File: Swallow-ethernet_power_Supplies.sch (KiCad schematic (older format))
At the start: 29 parts, among them P7 +5V_In, P8 V_In, U12 NCP1529, U13 NCP1529, U14 NCP303LSN09T1G

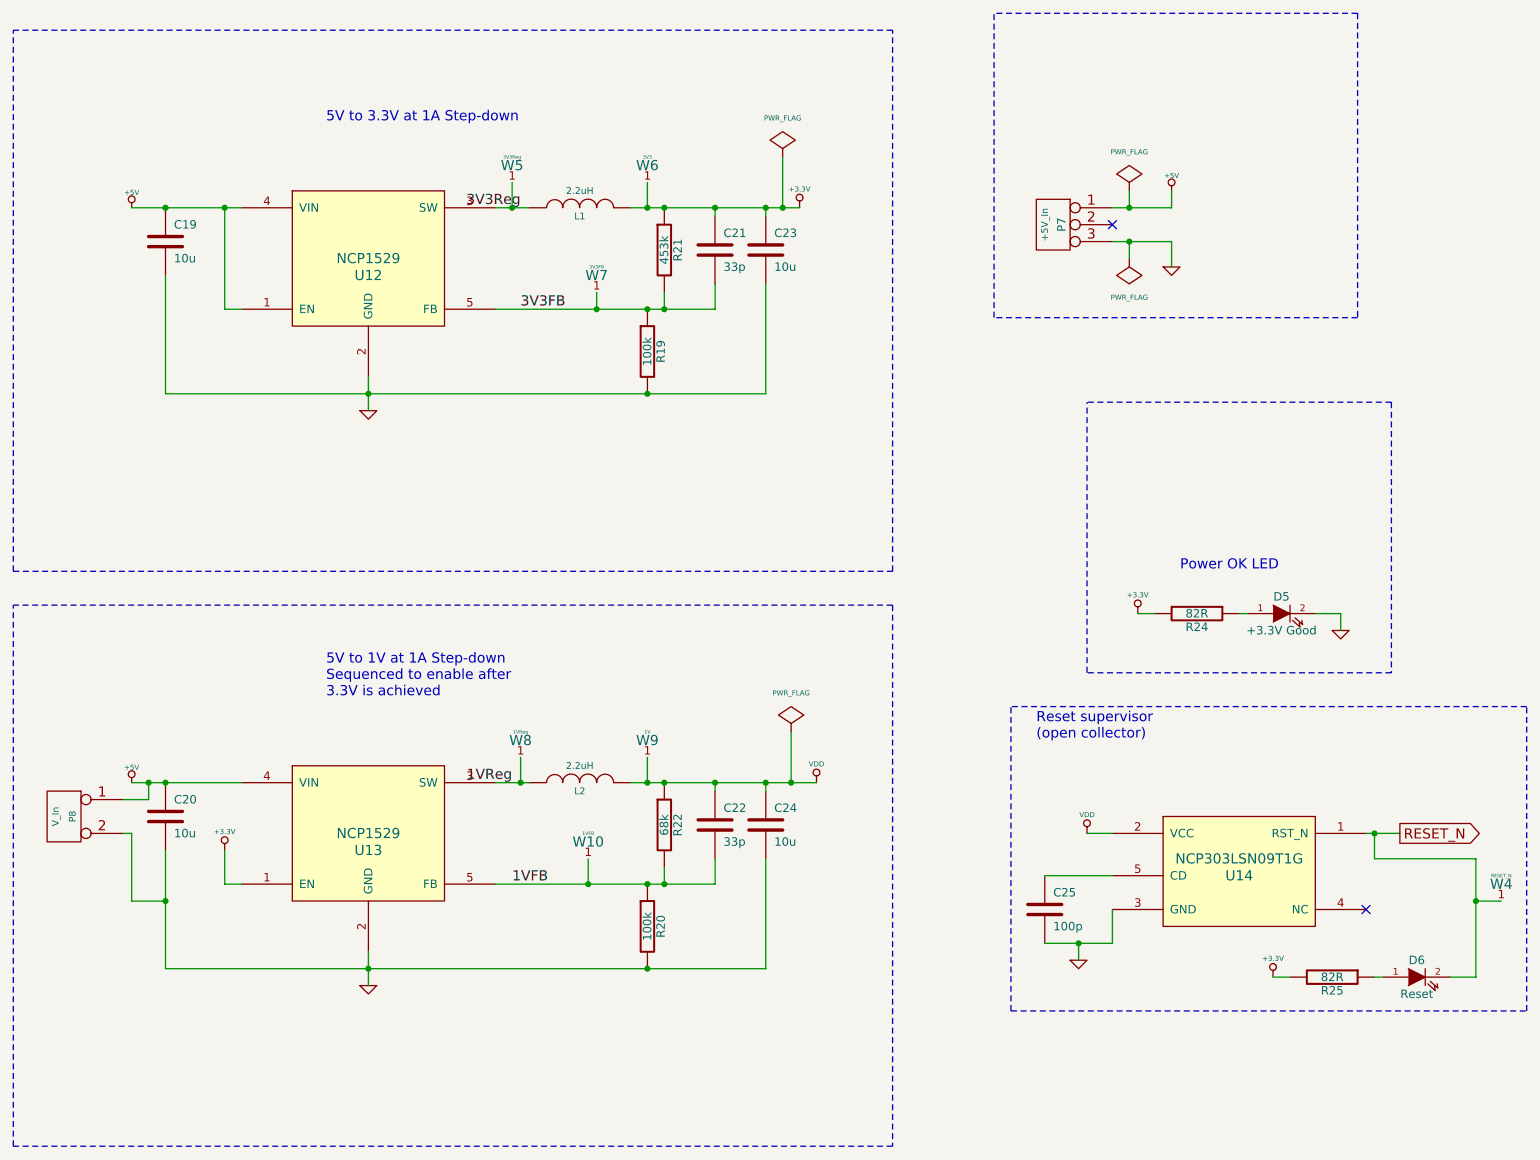
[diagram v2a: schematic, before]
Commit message: Re-annotated schematic and deleted redundant components from PCB design.
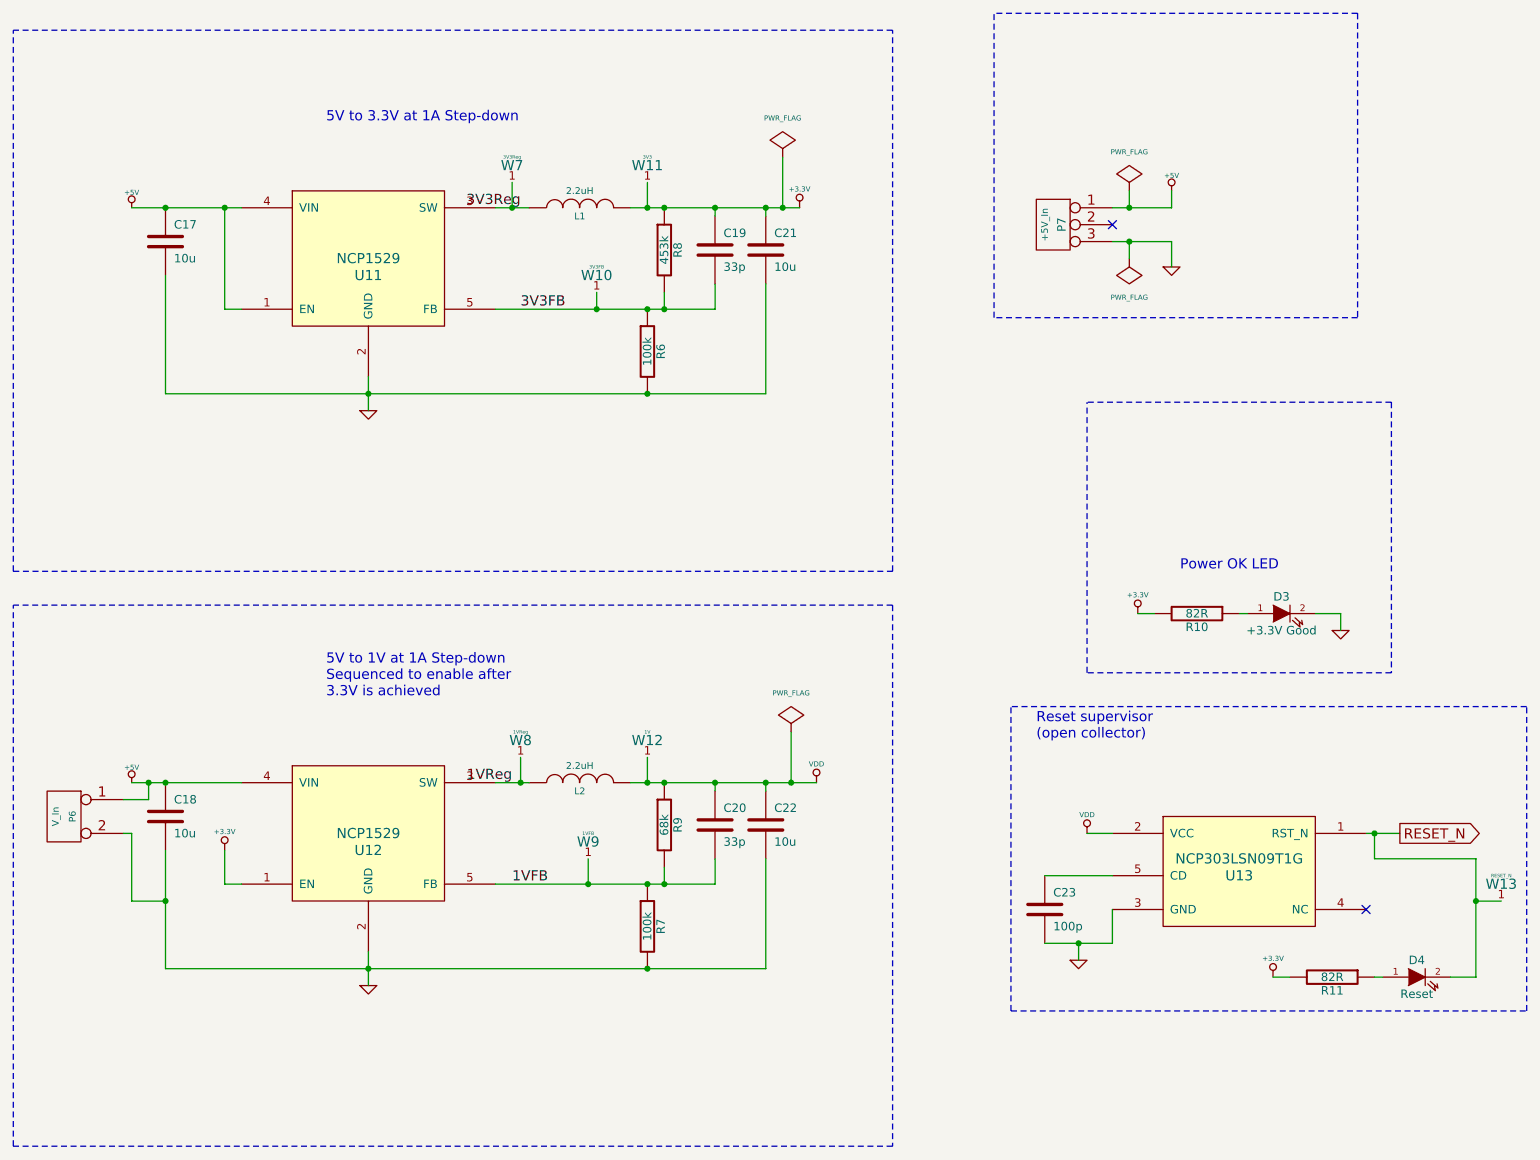
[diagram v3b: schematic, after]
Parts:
- renumbered C19 to C17, C20 to C18, C21 to C19, C22 to C20, C23 to C21, C24 to C22, C25 to C23, D5 to D3, D6 to D4, P8 to P6, R24 to R10, R25 to R11, R19 to R6, R20 to R7, R21 to R8, R22 to R9, U12 to U11, U13 to U12, U14 to U13, W7 to W10, W6 to W11, W9 to W12, W4 to W13, W5 to W7, W10 to W9
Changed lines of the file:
@@
-EESchema Schematic File Version 2  date 30/09/2012 22:11:50
+EESchema Schematic File Version 2  date 30/09/2012 22:23:08
 LIBS:power
 LIBS:device
@@
 NoConn ~ 7550 2100
 $Comp
-L CONN_2 P8
+L CONN_2 P6
 U 1 1 4F69BE5A
 P 1350 5600
-F 0 "P8" V 1300 5600 40  0000 C CNN
+F 0 "P6" V 1300 5600 40  0000 C CNN
 F 1 "V_In" V 1400 5600 40  0000 C CNN
 	1    1350 5600
@@
 $EndComp
 $Comp
-L TESTPOINT W10
+L TESTPOINT W9
 U 1 1 4F5FB79A
 P 4450 5700
-F 0 "W10" H 4450 5650 60  0000 C CNN
+F 0 "W9" H 4450 5650 60  0000 C CNN
 F 1 "1VFB" H 4450 5700 20  0000 C CNN
 F 2 "TestPad-1mm" H 4450 5800 20  0001 C CNN
@@
 $EndComp
 $Comp
-L TESTPOINT W9
+L TESTPOINT W12
 U 1 1 4F5FB796
 P 4800 5100
-F 0 "W9" H 4800 5050 60  0000 C CNN
+F 0 "W12" H 4800 5050 60  0000 C CNN
 F 1 "1V" H 4800 5100 20  0000 C CNN
 F 2 "TestPad-1mm" H 4800 5200 20  0001 C CNN
@@
 $EndComp
 $Comp
-L TESTPOINT W7
+L TESTPOINT W10
 U 1 1 4F5FB764
 P 4500 2350
-F 0 "W7" H 4500 2300 60  0000 C CNN
+F 0 "W10" H 4500 2300 60  0000 C CNN
 F 1 "3V3FB" H 4500 2350 20  0000 C CNN
 F 2 "TestPad-1mm" H 4500 2450 20  0001 C CNN
@@
 $EndComp
 $Comp
-L TESTPOINT W6
+L TESTPOINT W11
 U 1 1 4F5FB75E
 P 4800 1700
-F 0 "W6" H 4800 1650 60  0000 C CNN
+F 0 "W11" H 4800 1650 60  0000 C CNN
 F 1 "3V3" H 4800 1700 20  0000 C CNN
 F 2 "TestPad-1mm" H 4800 1800 20  0001 C CNN
@@
 $EndComp
 $Comp
-L TESTPOINT W5
+L TESTPOINT W7
 U 1 1 4F5FB74C
 P 4000 1700
-F 0 "W5" H 4000 1650 60  0000 C CNN
+F 0 "W7" H 4000 1650 60  0000 C CNN
 F 1 "3V3Reg" H 4000 1700 20  0000 C CNN
 F 2 "TestPad-1mm" H 4000 1800 20  0001 C CNN
@@
 $EndComp
 $Comp
-L +3.3V #PWR085
+L +3.3V #PWR061
 U 1 1 4F5FB6A5
 P 2300 5800
-F 0 "#PWR085" H 2300 5760 30  0001 C CNN
+F 0 "#PWR061" H 2300 5760 30  0001 C CNN
 F 1 "+3.3V" H 2300 5910 30  0000 C CNN
 	1    2300 5800
@@
 1VReg
 $Comp
-L TESTPOINT W4
+L TESTPOINT W13
 U 1 1 4F5B5145
 P 9850 5950
-F 0 "W4" H 9850 5900 60  0000 C CNN
+F 0 "W13" H 9850 5900 60  0000 C CNN
 F 1 "RESET_N" H 9850 5950 20  0000 C CNN
 F 2 "TestPad-1mm" H 9850 6050 20  0001 C CNN
@@
 $EndComp
 $Comp
-L R R25
+L R R11
 U 1 1 4F5B50F0
 P 8850 6550
-F 0 "R25" V 8930 6550 50  0000 C CNN
+F 0 "R11" V 8930 6550 50  0000 C CNN
 F 1 "82R" V 8850 6550 50  0000 C CNN
 F 2 "SM0402" H 8850 6550 60  0001 C CNN
@@
 $EndComp
 $Comp
-L LED D6
+L LED D4
 U 1 1 4F5B50EF
 P 9350 6550
-F 0 "D6" H 9350 6650 50  0000 C CNN
+F 0 "D4" H 9350 6650 50  0000 C CNN
 F 1 "Reset" H 9350 6450 50  0000 C CNN
 F 2 "X_LED-0603" H 9350 6550 60  0001 C CNN
@@
 $EndComp
 $Comp
-L +3.3V #PWR086
+L +3.3V #PWR062
 U 1 1 4F5B50EE
 P 8500 6550
-F 0 "#PWR086" H 8500 6510 30  0001 C CNN
+F 0 "#PWR062" H 8500 6510 30  0001 C CNN
 F 1 "+3.3V" H 8500 6660 30  0000 C CNN
 	1    8500 6550
@@
 $EndComp
 $Comp
-L VDD #PWR087
+L VDD #PWR063
 U 1 1 4ED160AA
 P 5800 5400
-F 0 "#PWR087" H 5800 5500 30  0001 C CNN
+F 0 "#PWR063" H 5800 5500 30  0001 C CNN
 F 1 "VDD" H 5800 5510 30  0000 C CNN
 	1    5800 5400
@@
 NoConn ~ 9050 6150
 $Comp
-L GND #PWR088
+L GND #PWR064
 U 1 1 4EDA727F
 P 7350 6450
-F 0 "#PWR088" H 7350 6450 30  0001 C CNN
+F 0 "#PWR064" H 7350 6450 30  0001 C CNN
 F 1 "GND" H 7350 6380 30  0001 C CNN
 	1    7350 6450
@@
 $EndComp
 $Comp
-L VDD #PWR089
+L VDD #PWR065
 U 1 1 4EDA7272
 P 7400 5700
-F 0 "#PWR089" H 7400 5800 30  0001 C CNN
+F 0 "#PWR065" H 7400 5800 30  0001 C CNN
 F 1 "VDD" H 7400 5810 30  0000 C CNN
 	1    7400 5700
@@
 $EndComp
 $Comp
-L C C25
+L C C23
 U 1 1 4EDA724A
 P 7150 6150
-F 0 "C25" H 7200 6250 50  0000 L CNN
+F 0 "C23" H 7200 6250 50  0000 L CNN
 F 1 "100p" H 7200 6050 50  0000 L CNN
 F 2 "SM0402" H 7150 6150 60  0001 C CNN
@@
 $EndComp
 $Comp
-L NCP303 U14
+L NCP303 U13
 U 1 1 4EDA70F3
 P 8300 5950
-F 0 "U14" H 8300 5950 60  0000 C CNN
+F 0 "U13" H 8300 5950 60  0000 C CNN
 F 1 "NCP303LSN09T1G" H 8300 6050 60  0000 C CNN
 F 2 "TSOP-5" H 8300 5950 60  0001 C CNN
@@
 $EndComp
 $Comp
-L NCP1529 U13
+L NCP1529 U12
 U 1 1 4ED16424
 P 3150 5750
-F 0 "U13" H 3150 5700 60  0000 C CNN
+F 0 "U12" H 3150 5700 60  0000 C CNN
 F 1 "NCP1529" H 3150 5800 60  0000 C CNN
 F 2 "TSOP-5" H 3150 5750 60  0001 C CNN
@@
 $EndComp
 $Comp
-L GND #PWR090
+L GND #PWR066
 U 1 1 4ED17487
 P 8900 4500
-F 0 "#PWR090" H 8900 4500 30  0001 C CNN
+F 0 "#PWR066" H 8900 4500 30  0001 C CNN
 F 1 "GND" H 8900 4430 30  0001 C CNN
 	1    8900 4500
@@
 $EndComp
 $Comp
-L +3.3V #PWR091
+L +3.3V #PWR067
 U 1 1 4ED17439
 P 7700 4400
-F 0 "#PWR091" H 7700 4360 30  0001 C CNN
+F 0 "#PWR067" H 7700 4360 30  0001 C CNN
 F 1 "+3.3V" H 7700 4510 30  0000 C CNN
 	1    7700 4400
@@
 $EndComp
 $Comp
-L LED D5
+L LED D3
 U 1 1 4ED17411
 P 8550 4400
-F 0 "D5" H 8550 4500 50  0000 C CNN
+F 0 "D3" H 8550 4500 50  0000 C CNN
 F 1 "+3.3V Good" H 8550 4300 50  0000 C CNN
 F 2 "X_LED-0603" H 8550 4400 60  0001 C CNN
@@
 $EndComp
 $Comp
-L R R24
+L R R10
 U 1 1 4ED17400
 P 8050 4400
-F 0 "R24" V 8130 4400 50  0000 C CNN
+F 0 "R10" V 8130 4400 50  0000 C CNN
 F 1 "82R" V 8050 4400 50  0000 C CNN
 F 2 "SM0402" H 8050 4400 60  0001 C CNN
@@
 $EndComp
 $Comp
-L PWR_FLAG #FLG093
+L PWR_FLAG #FLG068
 U 1 1 4ED16457
 P 5650 5100
-F 0 "#FLG093" H 5650 5370 30  0001 C CNN
+F 0 "#FLG068" H 5650 5370 30  0001 C CNN
 F 1 "PWR_FLAG" H 5650 5330 30  0000 C CNN
 	1    5650 5100
@@
 $EndComp
 $Comp
-L PWR_FLAG #FLG094
+L PWR_FLAG #FLG069
 U 1 1 4ED16447
 P 5600 1700
-F 0 "#FLG094" H 5600 1970 30  0001 C CNN
+F 0 "#FLG069" H 5600 1970 30  0001 C CNN
 F 1 "PWR_FLAG" H 5600 1930 30  0000 C CNN
 	1    5600 1700
@@
 $EndComp
 $Comp
-L NCP1529 U12
+L NCP1529 U11
 U 1 1 4ED16412
 P 3150 2350
-F 0 "U12" H 3150 2300 60  0000 C CNN
+F 0 "U11" H 3150 2300 60  0000 C CNN
 F 1 "NCP1529" H 3150 2400 60  0000 C CNN
 F 2 "TSOP-5" H 3150 2350 60  0001 C CNN
@@
 $EndComp
 $Comp
-L PWR_FLAG #FLG095
+L PWR_FLAG #FLG070
 U 1 1 4ED162B6
 P 7650 2300
-F 0 "#FLG095" H 7650 2570 30  0001 C CNN
+F 0 "#FLG070" H 7650 2570 30  0001 C CNN
 F 1 "PWR_FLAG" H 7650 2530 30  0000 C CNN
 	1    7650 2300
@@
 $EndComp
 $Comp
-L PWR_FLAG #FLG096
+L PWR_FLAG #FLG071
 U 1 1 4ED16176
 P 7650 1900
-F 0 "#FLG096" H 7650 2170 30  0001 C CNN
+F 0 "#FLG071" H 7650 2170 30  0001 C CNN
 F 1 "PWR_FLAG" H 7650 2130 30  0000 C CNN
 	1    7650 1900
@@
 $EndComp
 $Comp
-L +5V #PWR097
+L +5V #PWR072
 U 1 1 4ED1613C
 P 7900 1900
-F 0 "#PWR097" H 7900 1990 20  0001 C CNN
+F 0 "#PWR072" H 7900 1990 20  0001 C CNN
 F 1 "+5V" H 7900 1990 30  0000 C CNN
 	1    7900 1900
@@
 $EndComp
 $Comp
-L GND #PWR098
+L GND #PWR073
 U 1 1 4ED16138
 P 7900 2350
-F 0 "#PWR098" H 7900 2350 30  0001 C CNN
+F 0 "#PWR073" H 7900 2350 30  0001 C CNN
 F 1 "GND" H 7900 2280 30  0001 C CNN
 	1    7900 2350
@@
 $EndComp
 $Comp
-L C C20
+L C C18
 U 1 1 4ED16055
 P 1950 5600
-F 0 "C20" H 2000 5700 50  0000 L CNN
+F 0 "C18" H 2000 5700 50  0000 L CNN
 F 1 "10u" H 2000 5500 50  0000 L CNN
 F 2 "SM0805" H 1950 5600 60  0001 C CNN
@@
 $EndComp
 $Comp
-L GND #PWR099
+L GND #PWR074
 U 1 1 4ED16054
 P 3150 6600
-F 0 "#PWR099" H 3150 6600 30  0001 C CNN
+F 0 "#PWR074" H 3150 6600 30  0001 C CNN
 F 1 "GND" H 3150 6530 30  0001 C CNN
 	1    3150 6600
@@
 $EndComp
 $Comp
-L R R20
+L R R7
 U 1 1 4ED16053
 P 4800 6250
-F 0 "R20" V 4880 6250 50  0000 C CNN
+F 0 "R7" V 4880 6250 50  0000 C CNN
 F 1 "100k" V 4800 6250 50  0000 C CNN
 F 2 "SM0402" H 4800 6250 60  0001 C CNN
@@
 $EndComp
 $Comp
-L R R22
+L R R9
 U 1 1 4ED16052
 P 4900 5650
-F 0 "R22" V 4980 5650 50  0000 C CNN
+F 0 "R9" V 4980 5650 50  0000 C CNN
 F 1 "68k" V 4900 5650 50  0000 C CNN
 F 2 "SM0402" H 4900 5650 60  0001 C CNN
@@
 $EndComp
 $Comp
-L C C22
+L C C20
 U 1 1 4ED16050
 P 5200 5650
-F 0 "C22" H 5250 5750 50  0000 L CNN
+F 0 "C20" H 5250 5750 50  0000 L CNN
 F 1 "33p" H 5250 5550 50  0000 L CNN
 F 2 "SM0603" H 5200 5650 60  0001 C CNN
@@
 $EndComp
 $Comp
-L C C24
+L C C22
 U 1 1 4ED1604F
 P 5500 5650
-F 0 "C24" H 5550 5750 50  0000 L CNN
+F 0 "C22" H 5550 5750 50  0000 L CNN
 F 1 "10u" H 5550 5550 50  0000 L CNN
 F 2 "SM0805" H 5500 5650 60  0001 C CNN
@@
 $EndComp
 $Comp
-L +5V #PWR0100
+L +5V #PWR075
 U 1 1 4ED1604D
 P 1750 5400
-F 0 "#PWR0100" H 1750 5490 20  0001 C CNN
+F 0 "#PWR075" H 1750 5490 20  0001 C CNN
 F 1 "+5V" H 1750 5490 30  0000 C CNN
 	1    1750 5400
@@
 5V to 3.3V at 1A Step-down
 $Comp
-L +5V #PWR0101
+L +5V #PWR076
 U 1 1 4ED15FDA
 P 1750 2000
-F 0 "#PWR0101" H 1750 2090 20  0001 C CNN
+F 0 "#PWR076" H 1750 2090 20  0001 C CNN
 F 1 "+5V" H 1750 2090 30  0000 C CNN
 	1    1750 2000
@@
 $EndComp
 $Comp
-L +3.3V #PWR0102
+L +3.3V #PWR077
 U 1 1 4ED15FB8
 P 5700 2000
-F 0 "#PWR0102" H 5700 1960 30  0001 C CNN
+F 0 "#PWR077" H 5700 1960 30  0001 C CNN
 F 1 "+3.3V" H 5700 2110 30  0000 C CNN
 	1    5700 2000
@@
 $EndComp
 $Comp
-L C C23
+L C C21
 U 1 1 4ED15F6E
 P 5500 2250
-F 0 "C23" H 5550 2350 50  0000 L CNN
+F 0 "C21" H 5550 2350 50  0000 L CNN
 F 1 "10u" H 5550 2150 50  0000 L CNN
 F 2 "SM0805" H 5500 2250 60  0001 C CNN
@@
 $EndComp
 $Comp
-L C C21
+L C C19
 U 1 1 4ED15F6B
 P 5200 2250
-F 0 "C21" H 5250 2350 50  0000 L CNN
+F 0 "C19" H 5250 2350 50  0000 L CNN
 F 1 "33p" H 5250 2150 50  0000 L CNN
 F 2 "SM0603" H 5200 2250 60  0001 C CNN
@@
 $EndComp
 $Comp
-L R R21
+L R R8
 U 1 1 4ED15F38
 P 4900 2250
-F 0 "R21" V 4980 2250 50  0000 C CNN
+F 0 "R8" V 4980 2250 50  0000 C CNN
 F 1 "453k" V 4900 2250 50  0000 C CNN
 F 2 "SM0805" H 4900 2250 60  0001 C CNN
@@
 $EndComp
 $Comp
-L R R19
+L R R6
 U 1 1 4ED15F30
 P 4800 2850
-F 0 "R19" V 4880 2850 50  0000 C CNN
+F 0 "R6" V 4880 2850 50  0000 C CNN
 F 1 "100k" V 4800 2850 50  0000 C CNN
 F 2 "SM0402" H 4800 2850 60  0001 C CNN
@@
 $EndComp
 $Comp
-L GND #PWR0103
+L GND #PWR078
 U 1 1 4ED15EEA
 P 3150 3200
-F 0 "#PWR0103" H 3150 3200 30  0001 C CNN
+F 0 "#PWR078" H 3150 3200 30  0001 C CNN
 F 1 "GND" H 3150 3130 30  0001 C CNN
 	1    3150 3200
@@
 $EndComp
 $Comp
-L C C19
+L C C17
 U 1 1 4ED15EDD
 P 1950 2200
-F 0 "C19" H 2000 2300 50  0000 L CNN
+F 0 "C17" H 2000 2300 50  0000 L CNN
 F 1 "10u" H 2000 2100 50  0000 L CNN
 F 2 "SM0805" H 1950 2200 60  0001 C CNN
